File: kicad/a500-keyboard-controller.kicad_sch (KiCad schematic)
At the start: 36 parts, among them J1 ICSP, J2 keyboard_matrix, J3 Mainboard, Q1 BC547, U1 PIC18F4520

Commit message: updated BOM
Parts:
- C1, C2: MPN (none) -> A104K15X7RF5UAA; Manufacturer (none) -> Vishay
- C3, C4: MPN (none) -> D102K20Y5PH63J5R; Manufacturer (none) -> Vishay
- C5: MPN (none) -> EEA-GA1C220H; Manufacturer (none) -> Panasonic
- J1, J3, TP1: now left out of the parts list
- J2: MPN (none) -> 39-53-2315; Manufacturer (none) -> Molex
- Q1: MPN (none) -> BC547C
- R1, R2, R3, R4, R5, R7: MPN (none) -> MF0207FTE52-47K; Manufacturer (none) -> Yageo
- R10: MPN (none) -> MF0207FTE52-1K8; Manufacturer (none) -> Yageo
- R12: MPN (none) -> MF0207FTE52-270R; Manufacturer (none) -> Yageo
- R13, R14, R8: MPN (none) -> MF0207FTE52-22R; Manufacturer (none) -> Yageo
- R6: MPN (none) -> MF0207FTE52-220R; Manufacturer (none) -> Yageo
- R9: MPN (none) -> MF0207FTE52-470R; Manufacturer (none) -> Yageo
- U1: MPN (none) -> PIC18F4520-I/P; Manufacturer (none) -> Microchip

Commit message: bigger footprint for bulk capacitor
bumped revision
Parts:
- C5: footprint Capacitor_THT:CP_Radial_D5.0mm_P2.00mm -> Capacitor_THT:CP_Radial_D6.3mm_P2.50mm
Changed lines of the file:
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@@
 	(title_block
 		(title "Mitsumi PCB A-500 Redone")
-		(date "2026-01-01")
-		(rev "1.0")
+		(date "2026-01-21")
+		(rev "1.1")
 		(company "Dennis van Weeren")
 	)
@@
 			)
 		)
-		(property "Footprint" "Capacitor_THT:CP_Radial_D5.0mm_P2.00mm"
+		(property "Footprint" "Capacitor_THT:CP_Radial_D6.3mm_P2.50mm"
 			(at 158.4452 124.46 0)
 			(effects

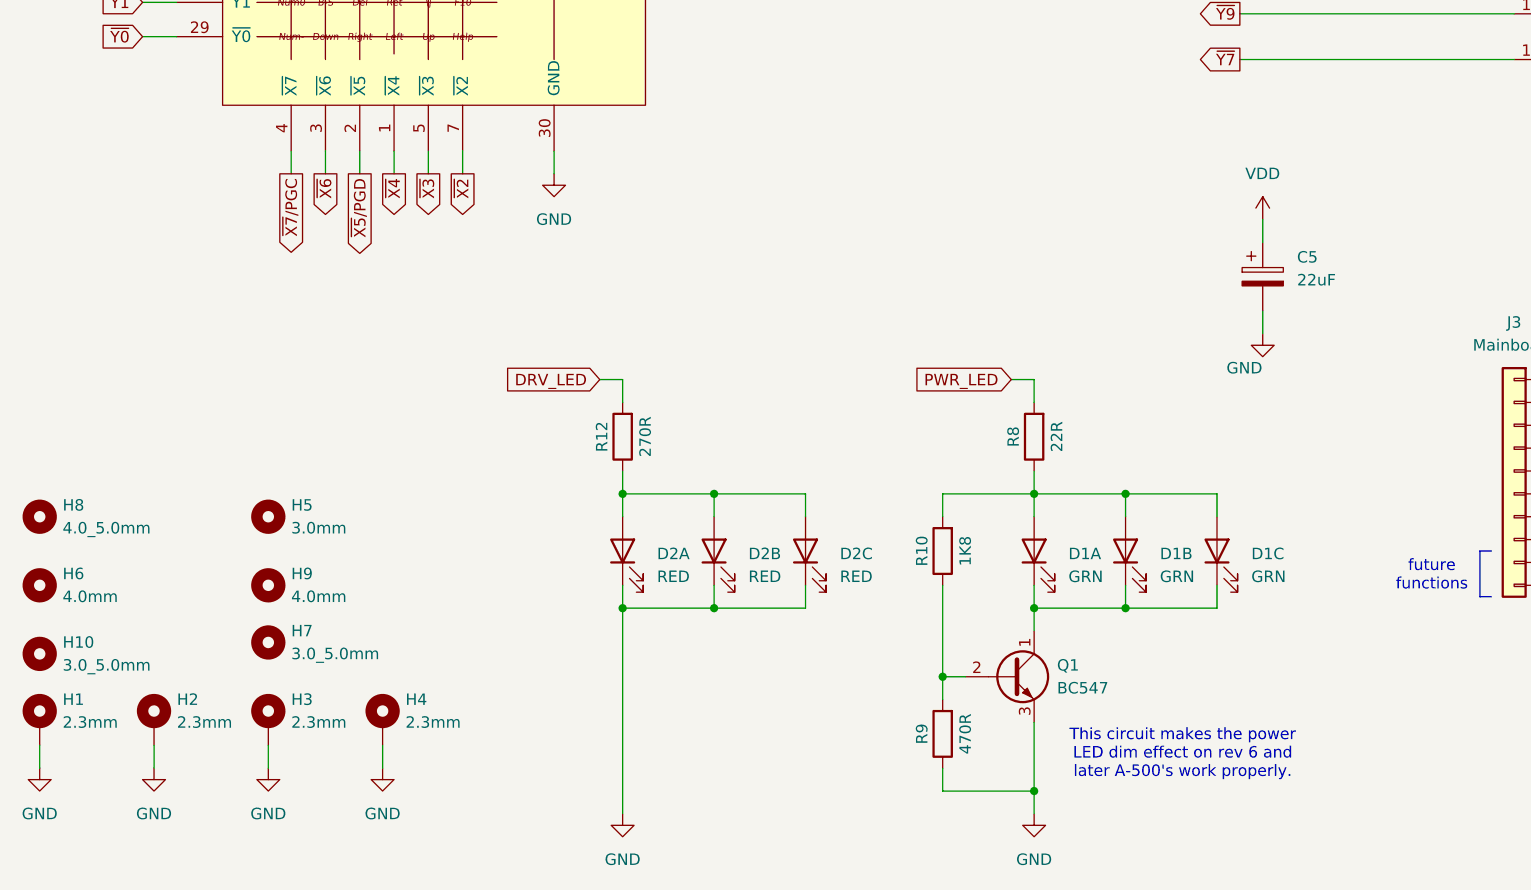
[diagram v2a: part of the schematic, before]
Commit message: host cable now connects to right angle pin header
This is version 1.1 and has been sent to production
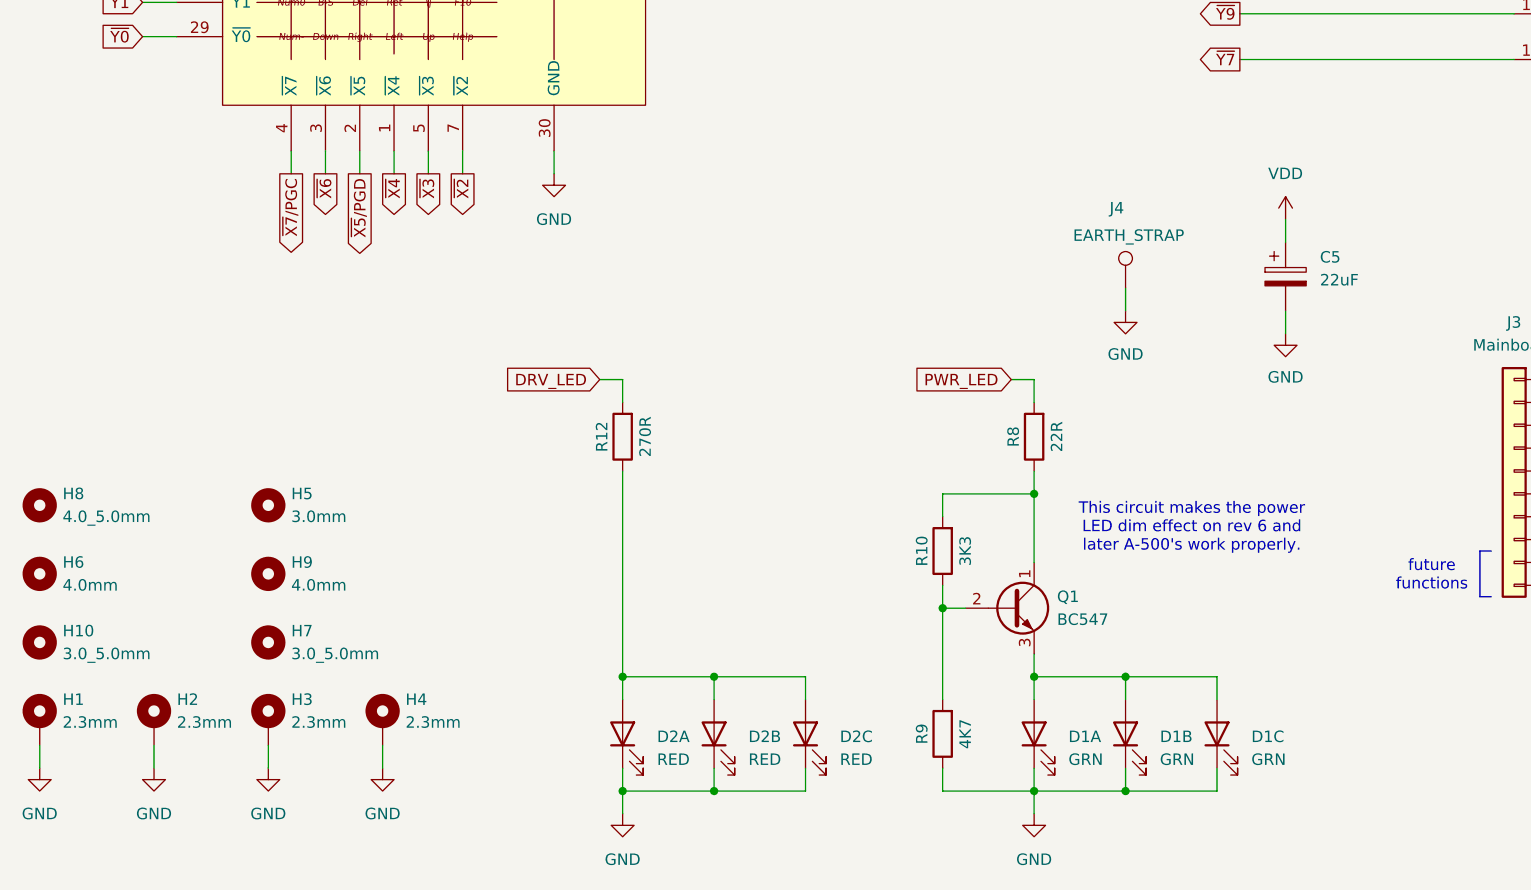
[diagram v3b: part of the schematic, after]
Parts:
- added J4: EARTH_STRAP, Connector_Wire:SolderWire-1.5sqmm_1x01_D1.7mm_OD3mm, symbol Connector:TestPoint
- J3: footprint Connector_PinHeader_2.54mm:PinHeader_1x10_P2.54mm_Vertical -> Connector_PinHeader_2.54mm:PinHeader_1x10_P2.54mm_Horizontal
- R10: value 1K8 -> 3K3
- R9: value 470R -> 4K7
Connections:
- net GND: now also D1.1 (K), D1.3 (K), D1.5 (K), J4.1; no longer Q1.3 (E)
- net at D1.2 (A), D1.4 (A), D1.6 (A): now also Q1.3 (E); no longer R10.2, R8.1
- new net: Q1.1 (C), R10.2, R8.1
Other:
- moved on the sheet: C5, D1A, D1B, D1C, D2A, D2B, D2C, H10, H5, H6, H8, H9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

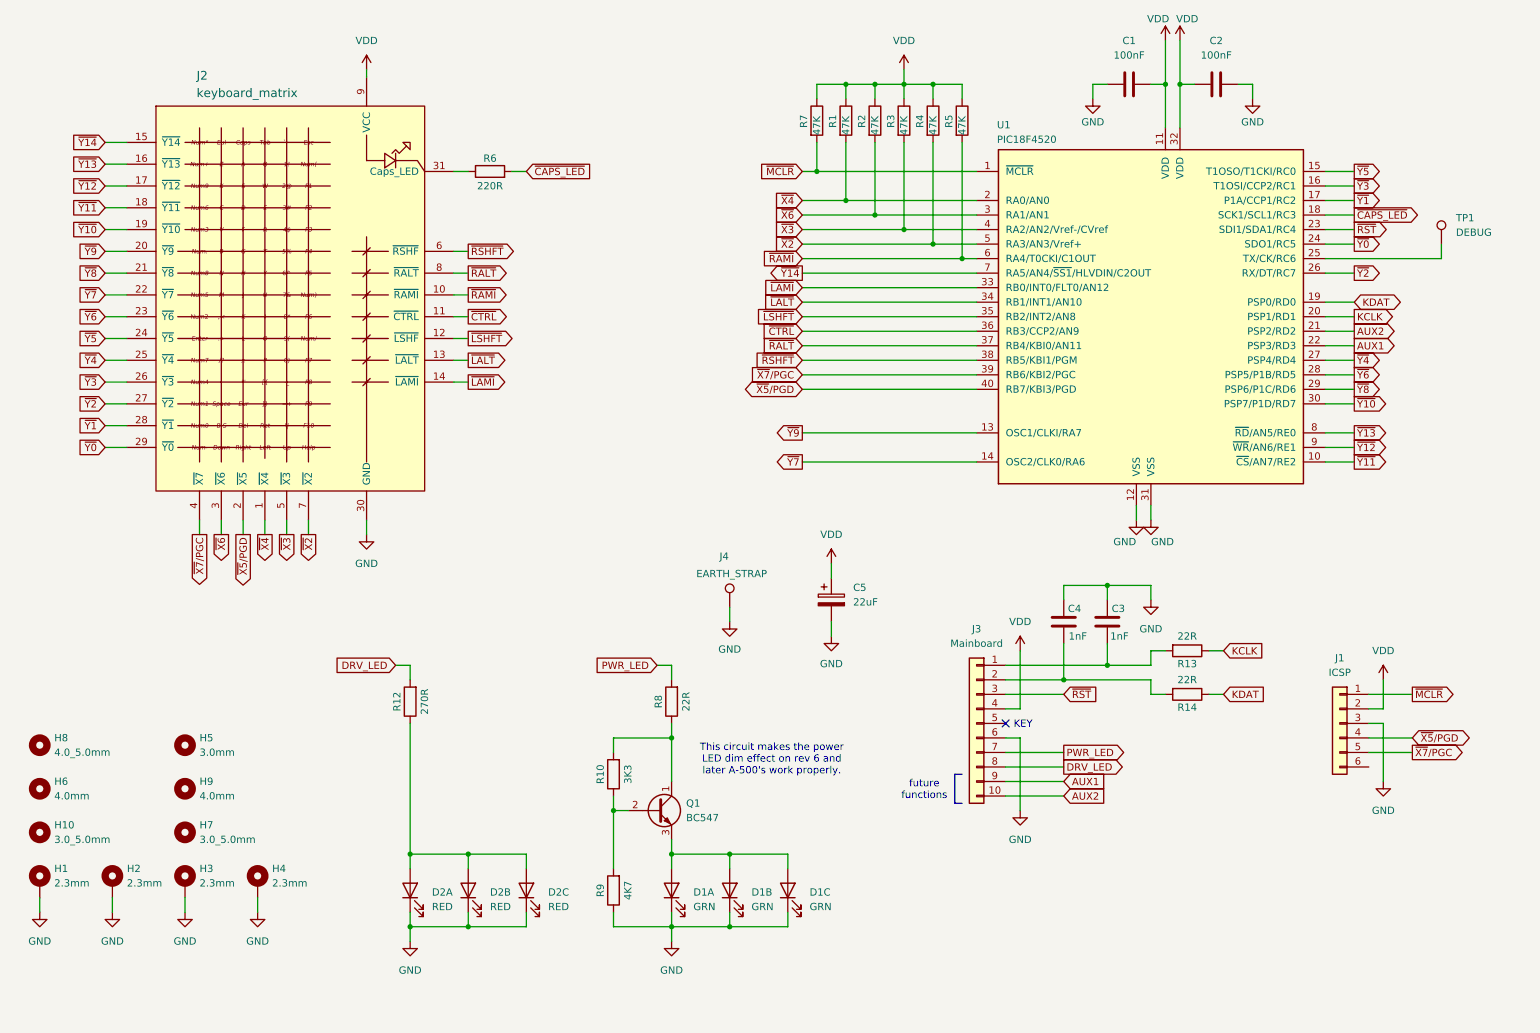
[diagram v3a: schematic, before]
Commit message: - fixed LED footprint dimensions
- completely reworked power LED circuit
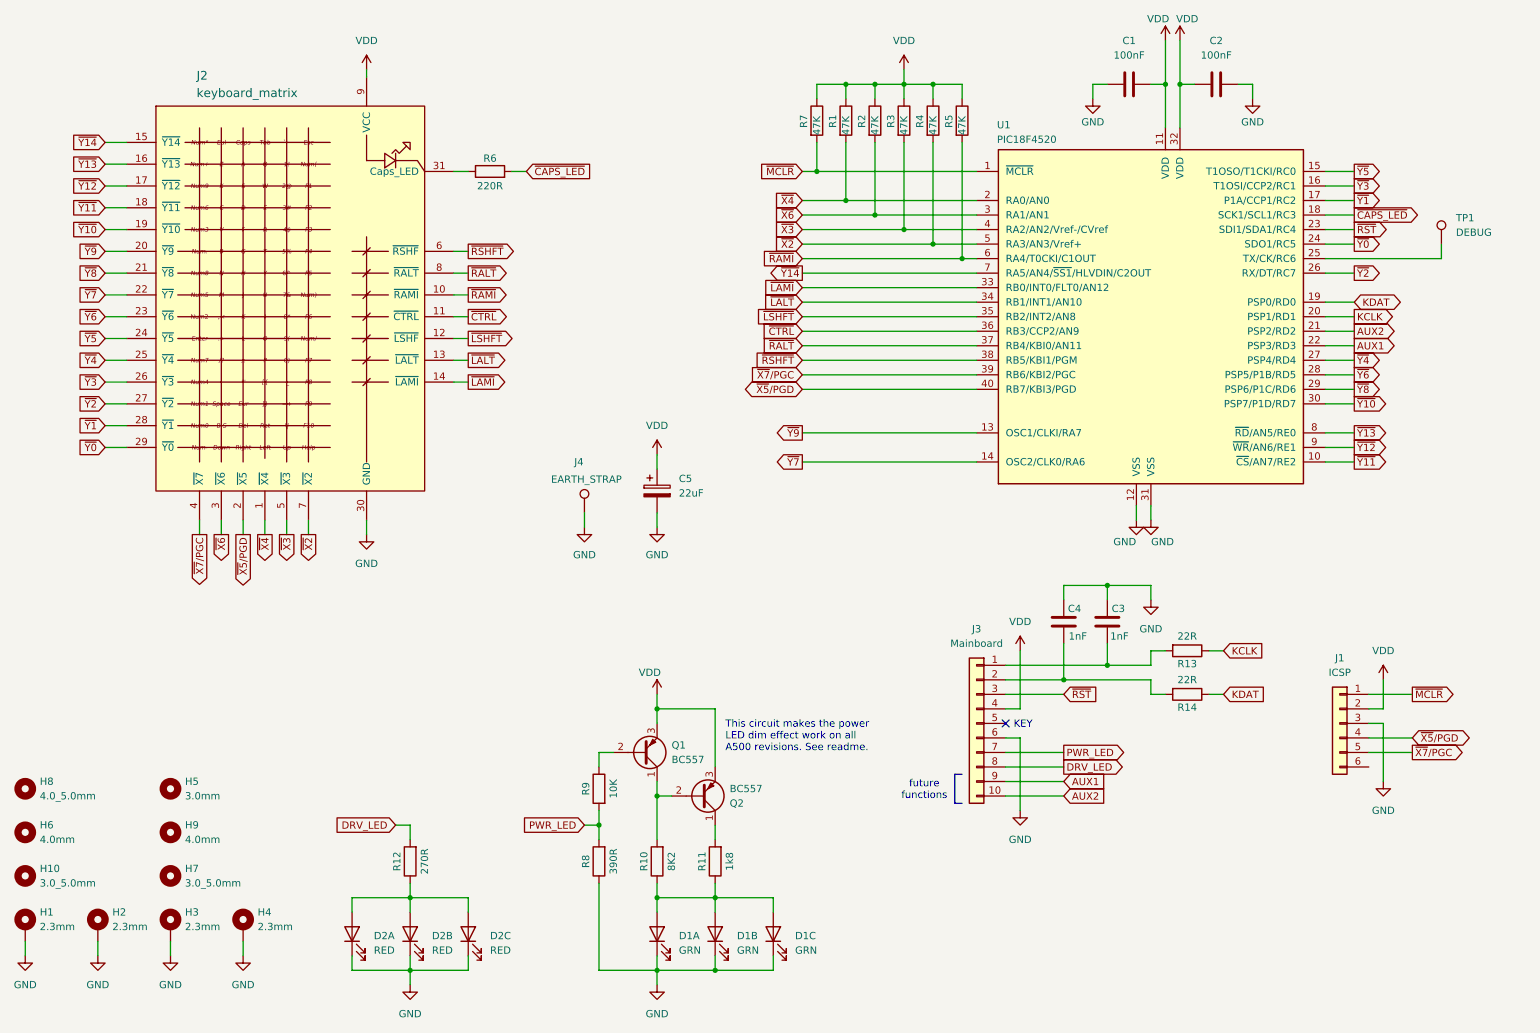
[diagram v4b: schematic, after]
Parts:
- removed Q1: BC547, Library:TO-92_HandSolder_modified, symbol Transistor_BJT:BC547
- added Q1, Q2: BC557, Library:TO-92_HandSolder_modified, symbol Transistor_BJT:BC557
- added R11: 1k8, Resistor_THT:R_Axial_DIN0207_L6.3mm_D2.5mm_P10.16mm_Horizontal, symbol Device:R
- R10: value 3K3 -> 8K2
- R8: value 22R -> 390R
- R9: value 4K7 -> 10K
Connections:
- net GND: now also R8.1; no longer R9.1
- net PWR_LED: now also R9.2
- net VDD: now also Q1.3 (E), Q2.3 (E)
- net at D1.2 (A), D1.4 (A), D1.6 (A): now also R10.1, R11.1
- net at R10.2: now also Q1.1 (C), Q2.2 (B); no longer R8.1
- new net: Q2.1 (C), R11.2
- new net: Q1.2 (B), R9.1
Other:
- note added: "This circuit makes the power LED dim effect work on all A500 revisions. See readme."
- note removed: "This circuit makes the power LED dim effect on rev 6 and later A-500's work properly."
- moved on the sheet: C5, D1A, D1B, D1C, D2A, D2B, D2C, H1, H10, H2, H3, H4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

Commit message: changed LED current limiting resistors values
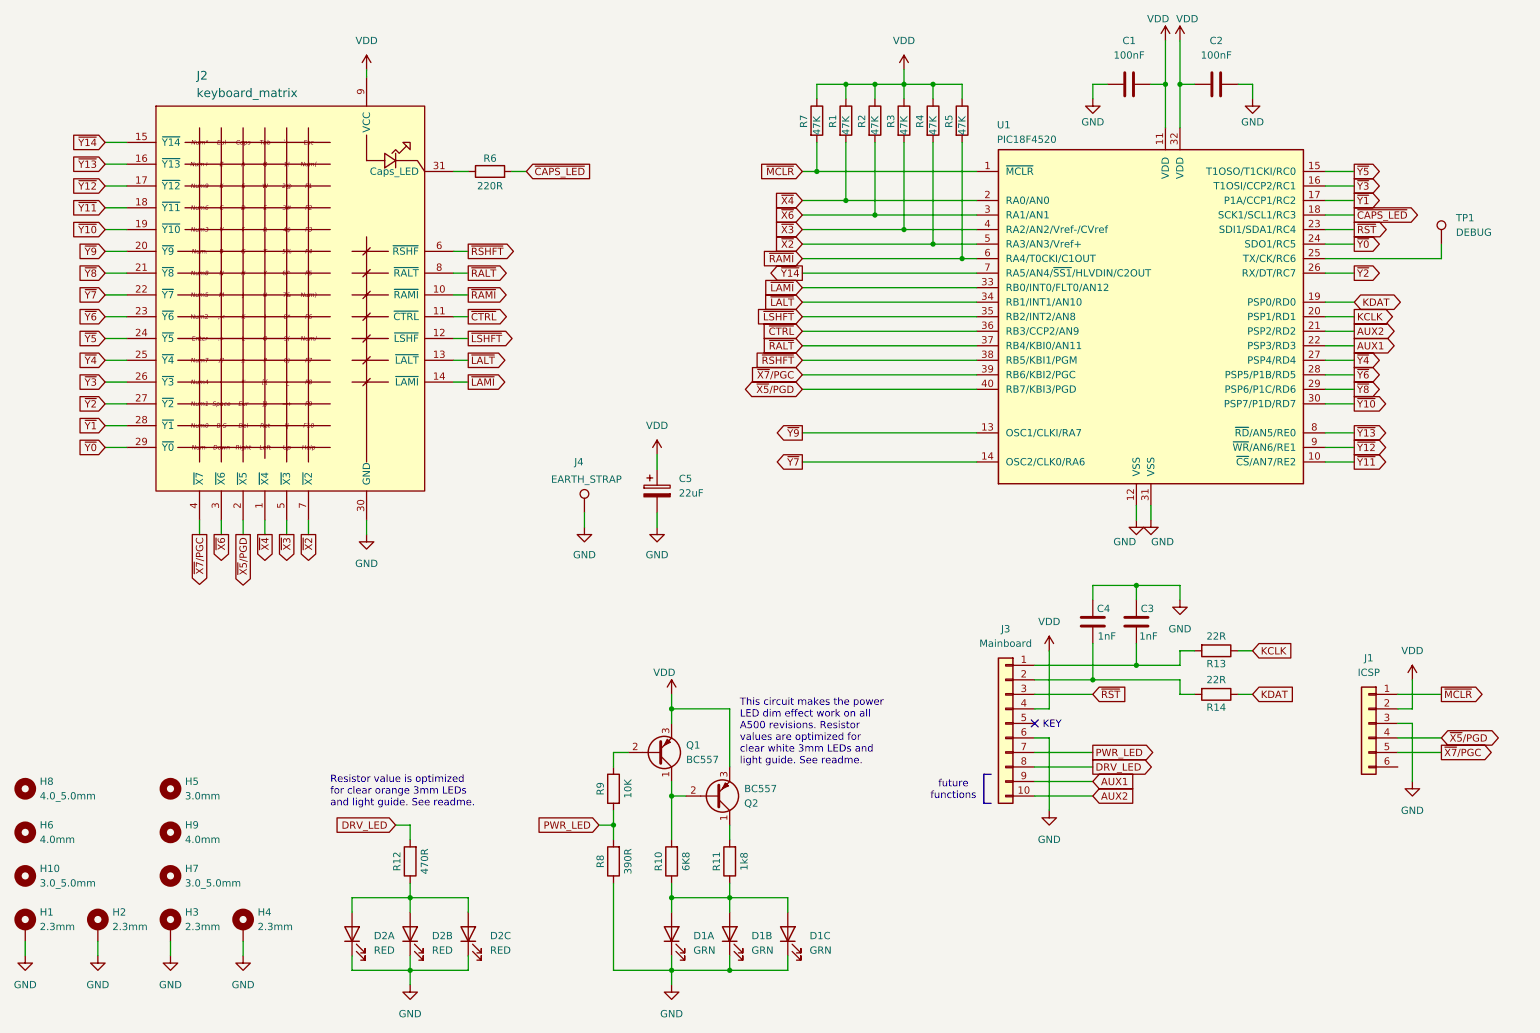
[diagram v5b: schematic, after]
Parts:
- R10: value 8K2 -> 6K8
- R12: value 270R -> 470R
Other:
- note added: "Resistor value is optimized for clear orange 3mm LEDs and light guide. See readme."
- note added: "This circuit makes the power LED dim effect work on all A500 revisions. Resistor values are optimized for clear white 3mm LEDs and light guide. See readme."
- note removed: "This circuit makes the power LED dim effect work on all A500 revisions. See readme."
- moved on the sheet: C3, C4, D1A, D1B, D1C, J1, J3, Q1, Q2, R10, R11, R13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

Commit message: updated some resistor partnumbers
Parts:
- R10: MPN MF0207FTE52-1K8 -> MF0207FTE52-6K8
- R12: MPN MF0207FTE52-270R -> MF0207FTE52-470R
- R8: MPN MF0207FTE52-22R -> MF0207FTE52-390R
- R9: MPN MF0207FTE52-470R -> MF0207FTE52-10K
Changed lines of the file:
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@@
 			)
 		)
-		(property "MPN" "MF0207FTE52-22R"
+		(property "MPN" "MF0207FTE52-390R"
 			(at 121.92 166.37 90)
 			(effects
@@
 			)
 		)
-		(property "MPN" "MF0207FTE52-270R"
+		(property "MPN" "MF0207FTE52-470R"
 			(at 86.36 166.37 90)
 			(effects
@@
 			)
 		)
-		(property "MPN" "MF0207FTE52-470R"
+		(property "MPN" "MF0207FTE52-10K"
 			(at 121.92 153.67 90)
 			(effects
@@
 			)
 		)
-		(property "MPN" "MF0207FTE52-1K8"
+		(property "MPN" "MF0207FTE52-6K8"
 			(at 132.08 166.37 90)
 			(effects
